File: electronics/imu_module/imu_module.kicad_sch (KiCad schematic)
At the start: 32 parts, among them J1 Conn_01x06_Male, J2 Conn_01x03_Male, J3 Conn_01x04, J4 Conn_01x04, U1 ESP32-WROOM-32U, U2 BMI088, U3 SN74LV1T34DBVR, U4 SP485, U5 AP2114HA-3.3TRG1

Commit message: library updates
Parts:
- removed L1: 22uH, lib:VLS5045EX330M, symbol Device:L
- removed PS1: PXO7805-500-M-TR, lib:CONV_PXO7805-500-M-TR, symbol PXO7805-500-M-TR:PXO7805-500-M-TR
- removed U3: SN74LV1T34DBVR, bitbots:SN74LV1T34DBVR, symbol SN74LV1T34DBVR:SN74LV1T34DBVR
- added L1: VLS5045EX-220M, lib:VLS5045EX330M, symbol VLS5045EX-220M:VLS5045EX-220M
- added PS2: PXO7805-500-M-TR, lib:PXO7805-500-M-TR, symbol PXO7805-500-M-TR:PXO7805-500-M-TR
- added U3: SN74LV1T34DBV, Package_TO_SOT_SMD:SOT-23-5, symbol Logic_LevelTranslator:SN74LV1T34DBV
- J1: footprint bitbots:testpoint_01x06 -> bitbots:esp32_pogo_programmer
- U2: footprint lib:PQFN50P450X300X100-16N -> lib:BMI088; DESCRIPTION Accelerometer, Gyroscope, 6 Axis Sensor I²C, SPI Output -> (none)
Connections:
- net +3V3: now also U3.5 (VCC); no longer J1.1 (Pin_1)
- net +5V: now also J1.1 (Pin_1), L1.2
- net GND: now also PS2.4 (GND), U3.3 (GND)
- net U2_RX: now also U3.4 (Y)
- net VBUS: now also PS2.1 (+VIN)
- net rs485_rx: now also U3.2 (A)
- net at C3.1: now also L1.1, PS2.3 (+VO)
- no-connect marks 18 -> 17
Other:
- moved on the sheet: C1, C10, C11, C2, C3, C4, C5, J1, J2, R1, U5

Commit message: prep for production
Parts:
- C1: LCSC Part # C1525 -> C13585
- C1, C2, C3, C4, C8: LCSC Part # C1525 -> C49678
- C10, C11: LCSC Part # C1525 -> C29823
- C3, C5: LCSC Part # C1525 -> C12891
- C5: LCSC Part # C1525 -> C15850
- H1, H2, H3, J2, JP1: now left out of the parts list
- J1: footprint bitbots:esp32_pogo_programmer -> lib:esp32_pogo_programmer; now left out of the parts list
- R1: LCSC Part # (none) -> C17414
- R2, R3: LCSC Part # (none) -> C17673
- U1: LCSC Part # (none) -> C3013937
- U2: LCSC Part # (none) -> C194919
- U3: LCSC Part # (none) -> C100024
- U4: LCSC Part # (none) -> C6855
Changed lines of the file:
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@@
 			)
 		)
-		(property "LCSC Part #" "C1525"
+		(property "LCSC Part #" "C49678"
 			(at 27.94 55.88 0)
 			(effects
@@
 			)
 		)
-		(property "LCSC Part #" "C1525"
+		(property "LCSC Part #" "C49678"
 			(at 165.1 46.99 0)
 			(effects
@@
 			)
 		)
-		(property "LCSC Part #" "C1525"
+		(property "LCSC Part #" "C15850"
 			(at 88.9 33.02 0)
 			(effects
@@
 			)
 		)
+		(property "LCSC Part #" "C17414"
+			(at 27.94 46.99 0)
+			(effects
+				(font
+					(size 1.27 1.27)
+				)
+				(hide yes)
+			)
+		)
 		(pin "1"
 		)
@@
 		(unit 1)
 		(exclude_from_sim no)
-		(in_bom yes)
+		(in_bom no)
 		(on_board yes)
 		(dnp no)
@@
 			)
 		)
-		(property "Footprint" "bitbots:esp32_pogo_programmer"
+		(property "Footprint" "lib:esp32_pogo_programmer"
 			(at 127 39.37 0)
 			(effects
@@
 			)
 		)
+		(property "LCSC Part #" "C3013937"
+			(at 52.07 82.55 0)
+			(effects
+				(font
+					(size 1.27 1.27)
+				)
+				(hide yes)
+			)
+		)
 		(pin "1"
 		)
@@
 			)
 		)
+		(property "LCSC Part #" "C6855"
+			(at 180.34 66.04 0)
+			(effects
+				(font
+					(size 1.27 1.27)
+				)
+				(hide yes)
+			)
+		)
 		(pin "1"
 		)
@@
 			)
 		)
-		(property "LCSC Part #" "C1525"
+		(property "LCSC Part #" "C49678"
 			(at 82.55 33.02 0)
 			(effects
@@
 		(unit 1)
 		(exclude_from_sim no)
-		(in_bom yes)
+		(in_bom no)
 		(on_board yes)
 		(dnp no)
@@
 		(unit 1)
 		(exclude_from_sim no)
-		(in_bom yes)
+		(in_bom no)
 		(on_board yes)
 		(dnp no)
@@
 		(unit 1)
 		(exclude_from_sim no)
-		(in_bom yes)
+		(in_bom no)
 		(on_board yes)
 		(dnp no)
@@
 			)
 		)
-		(property "LCSC Part #" "C1525"
+		(property "LCSC Part #" "C29823"
 			(at 259.08 147.32 0)
 			(effects
@@
 			)
 		)
-		(property "LCSC Part #" "C1525"
+		(property "LCSC Part #" "C29823"
 			(at 228.6 147.32 0)
 			(effects
@@
 			)
 		)
+		(property "LCSC Part #" "C17673"
+			(at 201.93 36.83 0)
+			(effects
+				(font
+					(size 1.27 1.27)
+				)
+				(hide yes)
+			)
+		)
 		(pin "1"
 		)
@@
 			)
 		)
-		(property "LCSC Part #" "C1525"
+		(property "LCSC Part #" "C13585"
 			(at 113.03 138.43 0)
 			(effects
@@
 			)
 		)
+		(property "LCSC Part #" "C194919"
+			(at 62.23 163.83 0)
+			(effects
+				(font
+					(size 1.27 1.27)
+				)
+				(hide yes)
+			)
+		)
 		(pin "2"
 		)
@@
 			)
 		)
-		(property "LCSC Part #" "C1525"
+		(property "LCSC Part #" "C12891"
 			(at 190.5 140.97 0)
 			(effects
@@
 		(unit 1)
 		(exclude_from_sim no)
-		(in_bom yes)
+		(in_bom no)
 		(on_board yes)
 		(dnp no)
@@
 		(unit 1)
 		(exclude_from_sim no)
-		(in_bom yes)
+		(in_bom no)
 		(on_board yes)
 		(dnp no)
@@
 			)
 		)
+		(property "LCSC Part #" "C100024"
+			(at 124.46 74.93 0)
+			(effects
+				(font
+					(size 1.27 1.27)
+				)
+				(hide yes)
+			)
+		)
 		(pin "4"
 		)
@@
 			)
 		)
-		(property "LCSC Part #" "C1525"
+		(property "LCSC Part #" "C49678"
 			(at 33.02 143.51 0)
 			(effects
@@
 			)
 		)
-		(property "LCSC Part #" "C1525"
+		(property "LCSC Part #" "C12891"
 			(at 153.67 140.97 0)
 			(effects
@@
 			)
 		)
+		(property "LCSC Part #" "C17673"
+			(at 201.93 44.45 0)
+			(effects
+				(font
+					(size 1.27 1.27)
+				)
+				(hide yes)
+			)
+		)
 		(pin "1"
 		)
@@
 			)
 		)
-		(property "LCSC Part #" "C1525"
+		(property "LCSC Part #" "C49678"
 			(at 25.4 143.51 0)
 			(effects

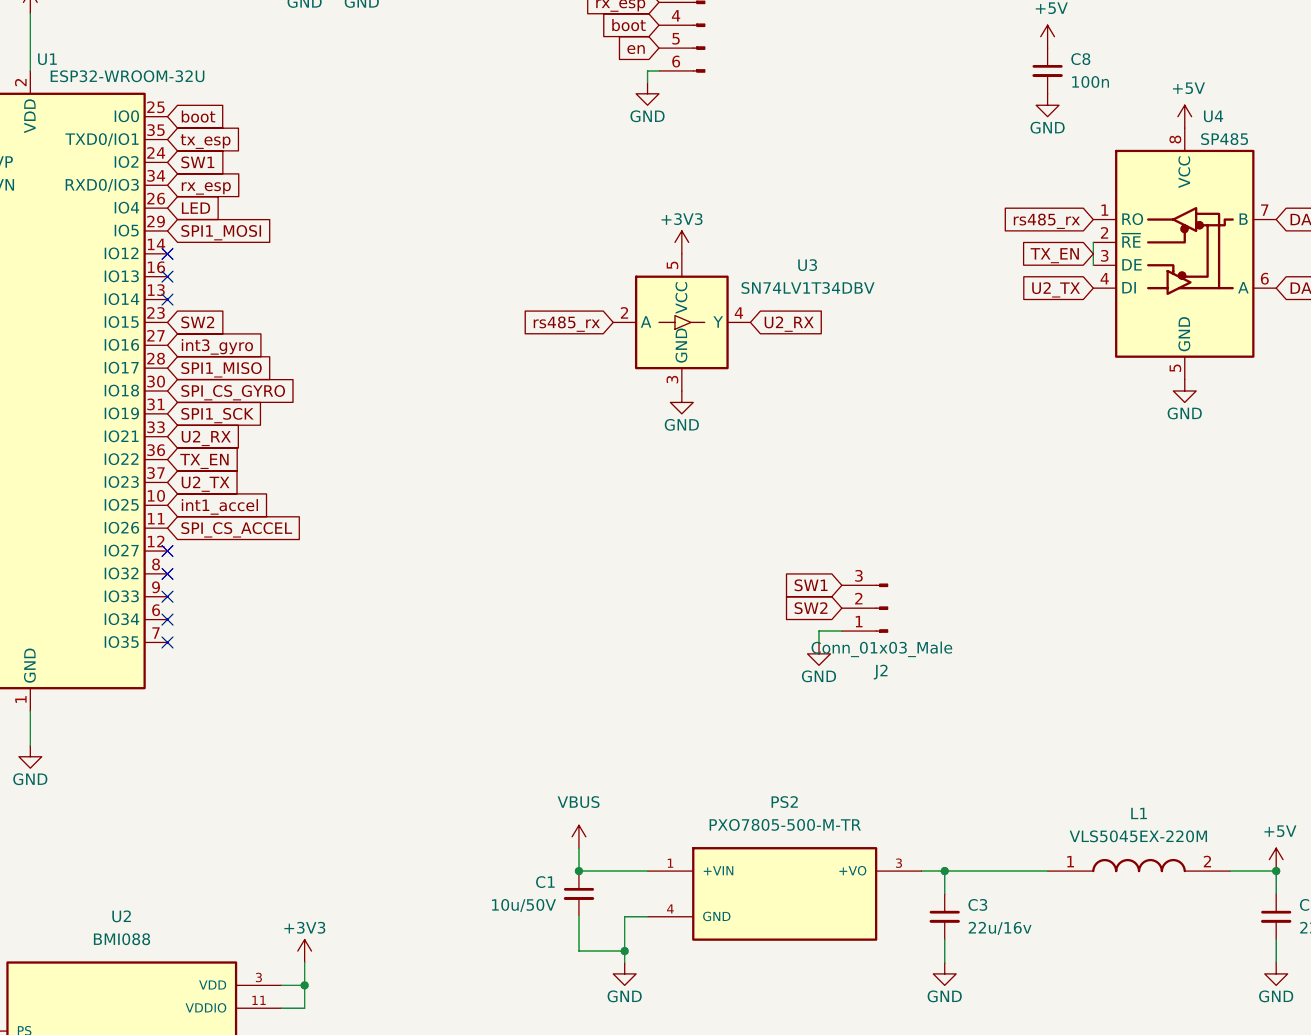
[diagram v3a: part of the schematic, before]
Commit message: new routing for buttons + leds on board
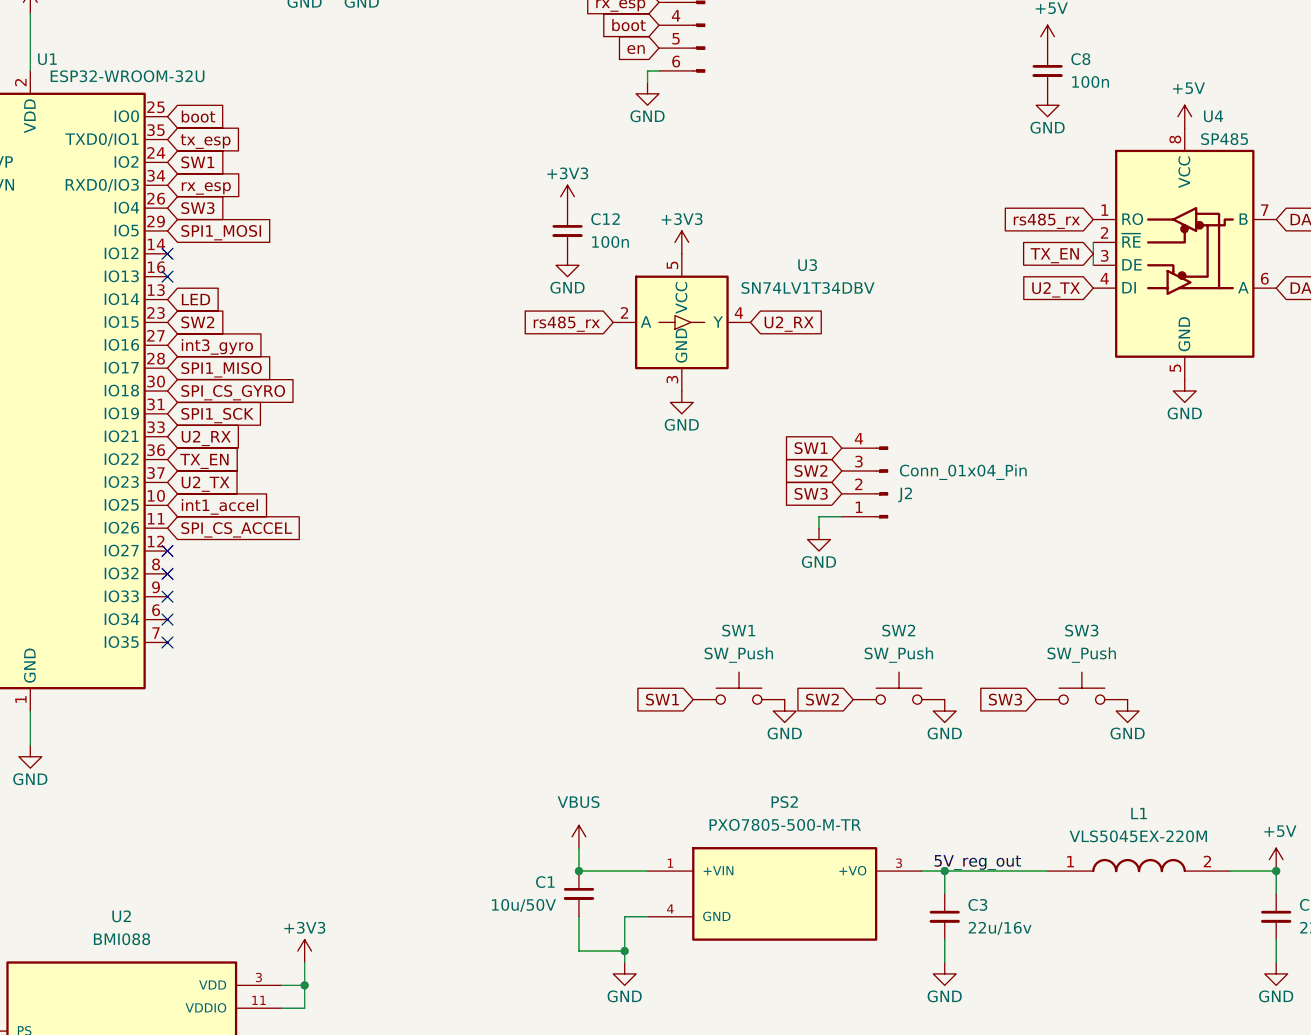
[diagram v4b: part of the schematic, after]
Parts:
- removed J2: Conn_01x03_Male, Connector_PinHeader_2.54mm:PinHeader_1x03_P2.54mm_Vertical, symbol Connector:Conn_01x03_Male
- added C12: 100n, Capacitor_SMD:C_0805_2012Metric, symbol Device:C_Small
- added J2: Conn_01x04_Pin, Connector_PinHeader_1.27mm:PinHeader_1x04_P1.27mm_Vertical, symbol Connector:Conn_01x04_Pin
- added SW1, SW2, SW3: SW_Push, lib:RND 210-00211, symbol Switch:SW_Push
- U1: footprint RF_Module:ESP32-WROOM-32U -> RF_Module:ESP32-WROOM-32UE
- U5: LCSC Part # (none) -> C460314
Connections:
- net +3V3: now also C12.1
- net GND: now also C12.2, J2.1 (Pin_1), SW1.2, SW2.2, SW3.2
- net LED: now also U1.13 (IO14); no longer U1.26 (IO4)
- net SW1: now also J2.4 (Pin_4), SW1.1
- net SW2: now also J2.3 (Pin_3), SW2.1
- net 5V_reg_out: now reaches C3.1, L1.1, PS2.3 (+VO)
- new net SW3: J2.2 (Pin_2), SW3.1, U1.26 (IO4)
- no-connect marks 17 -> 16

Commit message: production version and bom
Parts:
- removed J1: Conn_01x06_Male, lib:esp32_pogo_programmer, symbol Connector:Conn_01x06_Male
- removed PS2: PXO7805-500-M-TR, lib:PXO7805-500-M-TR, symbol PXO7805-500-M-TR:PXO7805-500-M-TR
- added J1: PRGM+Debug, lib:esp32_prgm_debug, symbol Connector_Generic:Conn_02x05_Counter_Clockwise
- added PS1: VXO7803-500-M / ROF-78E5.0-0.5SMD-R, lib:CONV_VXO7803-500-M, symbol VXO:VXO7803-500-M
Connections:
- net +5V: now also J1.1 (Pin_1)
- net 5V_reg_out: now also PS1.3 (+VO)
- net GND: now also J1.10 (Pin_10), PS1.2 (GND)
- net LED: now also U1.12 (IO27); no longer U1.13 (IO14)
- net SW2: now also U1.8 (IO32); no longer U1.23 (IO15)
- net VBUS: now also PS1.1 (+VIN)
- net boot: now also J1.4 (Pin_4)
- net en: now also J1.5 (Pin_5)
- net rx_esp: now also J1.3 (Pin_3)
- net tx_esp: now also J1.2 (Pin_2)
- net JTAG_MTDI: now reaches U1.14 (IO12)
- net JTAG_MTDI: now also J1.8 (Pin_8)
- net JTAG_MTCK: now reaches U1.16 (IO13)
- net JTAG_MTCK: now also J1.7 (Pin_7)
- new net JTAG_MTDO: J1.6 (Pin_6), U1.23 (IO15)
- new net JTAG_MTMS: J1.9 (Pin_9), U1.13 (IO14)
- no-connect marks 16 -> 13
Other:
- moved on the sheet: C1, C3, C5, L1
